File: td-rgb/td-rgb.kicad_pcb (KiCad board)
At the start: 2 copper layers, 65 x 29 mm, 26 parts, among them J1 ICD15S13E4GV00LF, J2 Conn_01x05_Male, J3 Conn_01x05_Male, J4 Conn_01x02_Male, SW1 SW_DPDT_x2, U1 LT1675CGNPBF, U2 LM2776

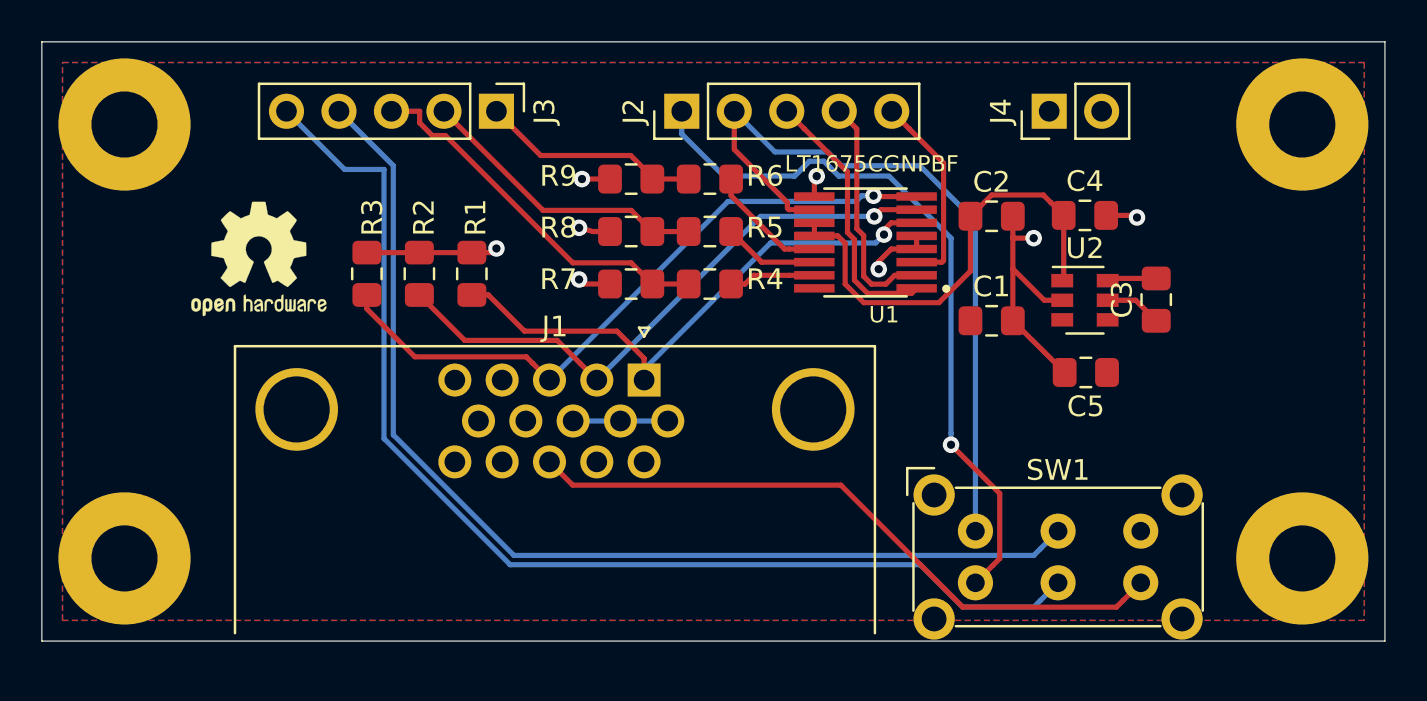
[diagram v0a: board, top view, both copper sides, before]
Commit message: Update footprint for DE-15 connector to correct pin row spacing
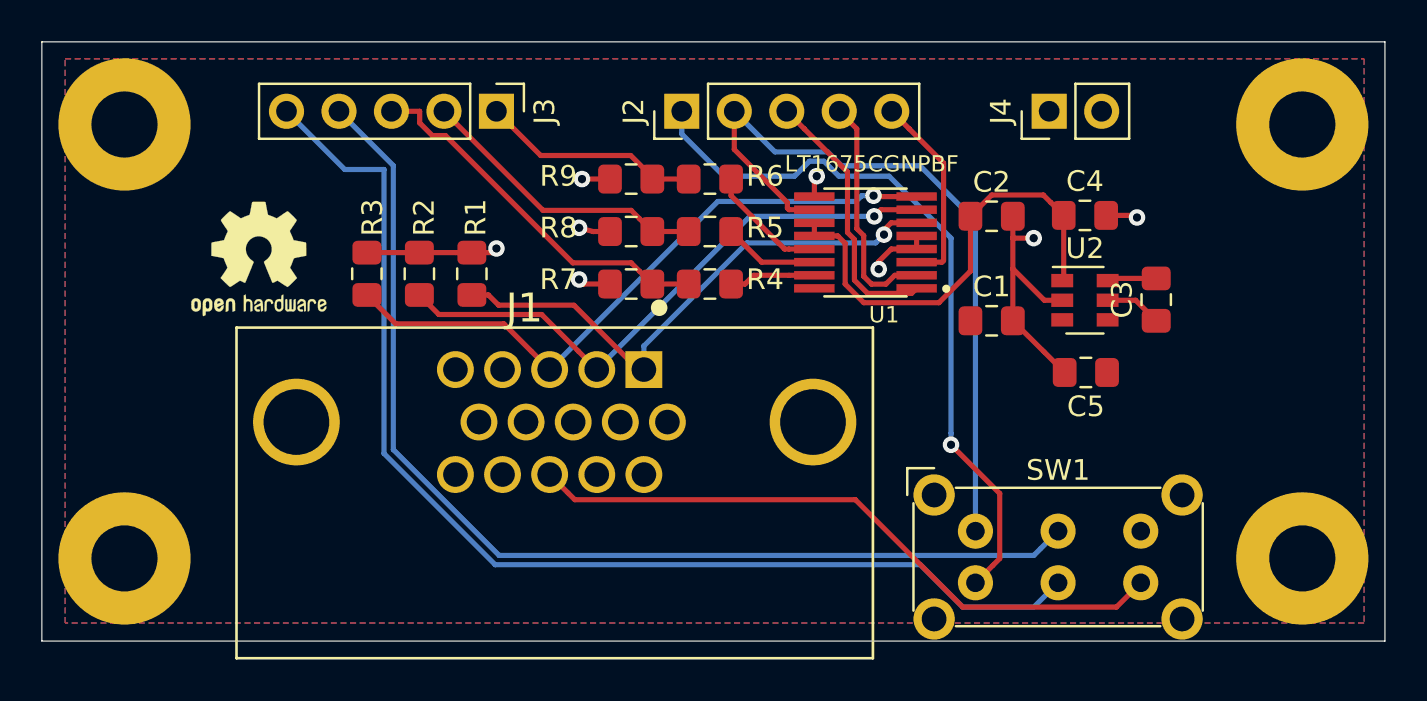
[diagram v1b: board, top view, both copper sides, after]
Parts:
- J1: footprint Connector_Dsub:DSUB-15-HD_Female_Horizontal_P2.29x1.98mm_EdgePinOffset8.35mm_Housed_MountingHolesOffset10.89mm -> 1-1734530-1:TE_1-1734530-1
- moved J1 4.78 mm to (134.8, 101.4)
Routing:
- net GND: track 33.7 -> 29.1 mm
- net /blue: track 32.4 -> 31.6 mm

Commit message: Correct DE-15 placement on PCB to bring closer to original design
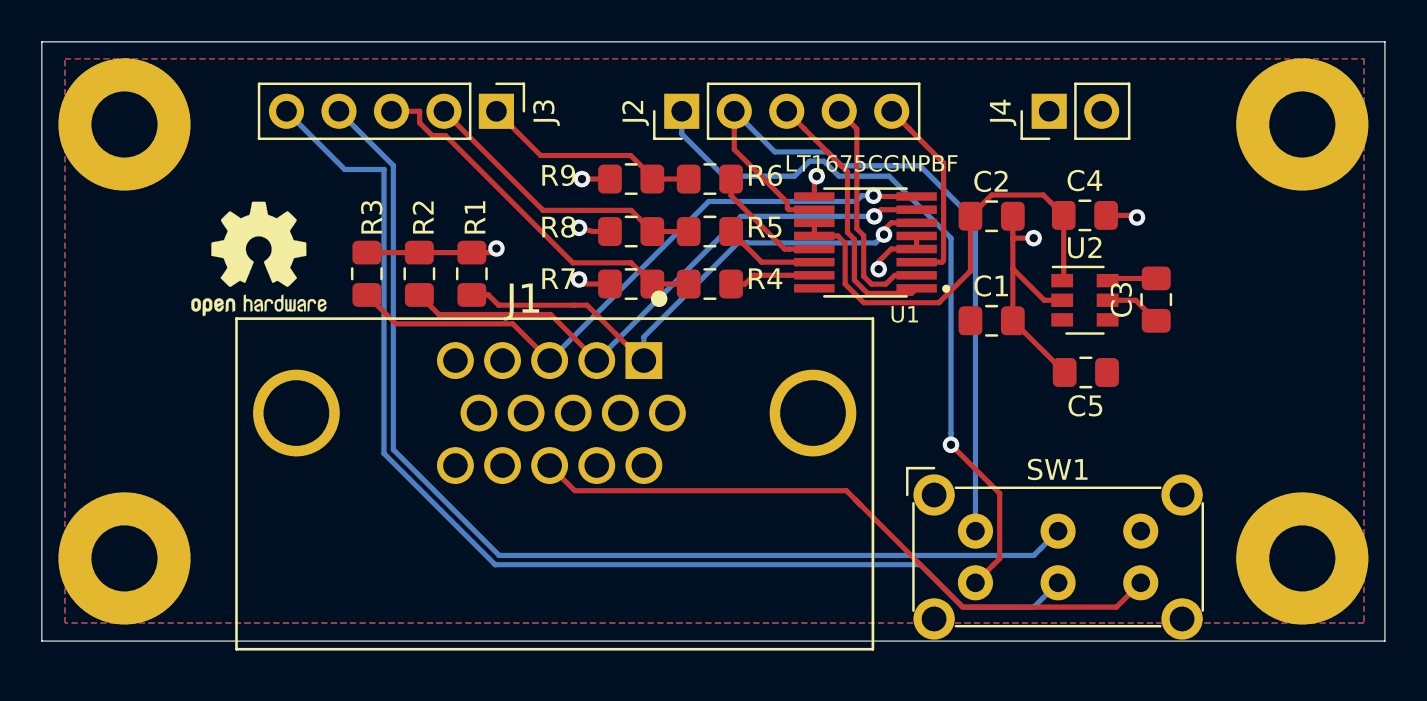
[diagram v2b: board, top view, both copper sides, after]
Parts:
- moved J1 0.44 mm to (134.8, 101.0)
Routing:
- net Net-(J1-Pad13): track 31.8 -> 32.3 mm
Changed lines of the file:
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@@
     (thickness 1.6)
     (drawings 19)
-    (tracks 184)
+    (tracks 187)
     (zones 0)
     (modules 26)
@@
   )
   (module 1-1734530-1:TE_1-1734530-1 (layer F.Cu)
-    (at 134.82 101.4)
+    (at 134.82 100.965)
     (fp_text reference J1 (at -1.47 -5.515) (layer F.SilkS)
       (effects (font (size 1.40272 1.40272) (thickness 0.05)))
@@
     (at 149.86 92.71 180)
     (attr smd)
-    (fp_text reference U1 (at -0.90029 -3.50115 180) (layer F.SilkS)
+    (fp_text reference U1 (at -1.905 -3.50115 180) (layer F.SilkS)
       (effects (font (size 0.787661 0.787661) (thickness 0.05)))
     )
@@
   (segment (start 148.52 92.3925) (end 148.874976 92.747476) (width 0.25) (layer F.Cu) (net 3))
   (segment (start 147.385 92.3925) (end 148.52 92.3925) (width 0.25) (layer F.Cu) (net 3))
-  (segment (start 135.467499 104.832499) (end 134.575 103.94) (width 0.25) (layer F.Cu) (net 6))
-  (segment (start 135.792501 105.157501) (end 135.467499 104.832499) (width 0.25) (layer F.Cu) (net 6))
-  (segment (start 149.370504 105.157501) (end 135.792501 105.157501) (width 0.25) (layer F.Cu) (net 6))
-  (segment (start 154.568004 110.355001) (end 149.370504 105.157501) (width 0.25) (layer F.Cu) (net 6))
   (segment (start 162.007 110.355001) (end 154.568004 110.355001) (width 0.25) (layer F.Cu) (net 6))
   (segment (start 163.182001 109.18) (end 162.007 110.355001) (width 0.25) (layer F.Cu) (net 6))
+  (segment (start 148.935504 104.722501) (end 149.623003 105.41) (width 0.25) (layer F.Cu) (net 6))
+  (segment (start 135.792501 104.722501) (end 148.935504 104.722501) (width 0.25) (layer F.Cu) (net 6))
+  (segment (start 134.575 103.505) (end 135.792501 104.722501) (width 0.25) (layer F.Cu) (net 6))
+  (segment (start 154.568004 110.355001) (end 149.623003 105.41) (width 0.25) (layer F.Cu) (net 6))
+  (segment (start 149.623003 105.41) (end 149.370504 105.157501) (width 0.25) (layer F.Cu) (net 6))
   (segment (start 152.335 90.4875) (end 150.291131 90.4875) (width 0.25) (layer F.Cu) (net 12))
   (segment (start 150.291131 90.4875) (end 150.250359 90.446728) (width 0.25) (layer F.Cu) (net 12))
   (via (at 150.250359 90.446728) (size 0.8) (drill 0.4) (layers F.Cu B.Cu) (net 12))
-  (segment (start 142.709999 90.725001) (end 134.575 98.86) (width 0.25) (layer B.Cu) (net 12))
-  (segment (start 149.406401 90.725001) (end 142.709999 90.725001) (width 0.25) (layer B.Cu) (net 12))
+  (segment (start 132.795732 96.645732) (end 134.575 98.425) (width 0.25) (layer F.Cu) (net 12))
+  (segment (start 125.73 95.25) (end 127.125732 96.645732) (width 0.25) (layer F.Cu) (net 12))
+  (segment (start 127.125732 96.645732) (end 132.795732 96.645732) (width 0.25) (layer F.Cu) (net 12))
+  (segment (start 142.274999 90.725001) (end 134.575 98.425) (width 0.25) (layer B.Cu) (net 12))
+  (segment (start 149.406401 90.725001) (end 142.274999 90.725001) (width 0.25) (layer B.Cu) (net 12))
   (segment (start 150.250359 90.446728) (end 149.684674 90.446728) (width 0.25) (layer B.Cu) (net 12))
   (segment (start 149.684674 90.446728) (end 149.406401 90.725001) (width 0.25) (layer B.Cu) (net 12))
-  (segment (start 133.682501 97.967501) (end 134.575 98.86) (width 0.25) (layer F.Cu) (net 12))
-  (segment (start 132.360732 96.645732) (end 133.682501 97.967501) (width 0.25) (layer F.Cu) (net 12))
-  (segment (start 127.125732 96.645732) (end 132.360732 96.645732) (width 0.25) (layer F.Cu) (net 12))
-  (segment (start 125.73 95.25) (end 127.125732 96.645732) (width 0.25) (layer F.Cu) (net 12))
   (segment (start 150.609696 91.1225) (end 150.286094 91.446102) (width 0.25) (layer F.Cu) (net 13))
   (via (at 150.286094 91.446102) (size 0.8) (drill 0.4) (layers F.Cu B.Cu) (net 13))
   (segment (start 152.335 91.1225) (end 150.609696 91.1225) (width 0.25) (layer F.Cu) (net 13))
-  (segment (start 144.268898 91.446102) (end 136.855 98.86) (width 0.25) (layer B.Cu) (net 13))
-  (segment (start 150.286094 91.446102) (end 144.268898 91.446102) (width 0.25) (layer B.Cu) (net 13))
-  (segment (start 135.962501 97.967501) (end 136.855 98.86) (width 0.25) (layer F.Cu) (net 13))
-  (segment (start 134.190722 96.195722) (end 135.962501 97.967501) (width 0.25) (layer F.Cu) (net 13))
-  (segment (start 129.215722 96.195722) (end 134.190722 96.195722) (width 0.25) (layer F.Cu) (net 13))
+  (segment (start 134.625722 96.195722) (end 136.855 98.425) (width 0.25) (layer F.Cu) (net 13))
   (segment (start 128.27 95.25) (end 129.215722 96.195722) (width 0.25) (layer F.Cu) (net 13))
+  (segment (start 129.215722 96.195722) (end 134.625722 96.195722) (width 0.25) (layer F.Cu) (net 13))
+  (segment (start 143.833898 91.446102) (end 136.855 98.425) (width 0.25) (layer B.Cu) (net 13))
+  (segment (start 150.286094 91.446102) (end 143.833898 91.446102) (width 0.25) (layer B.Cu) (net 13))
   (segment (start 152.335 91.7575) (end 151.105 91.7575) (width 0.25) (layer F.Cu) (net 14))
   (segment (start 151.105 91.7575) (end 150.754988 92.107512) (width 0.25) (layer F.Cu) (net 14))
   (via (at 150.754988 92.329357) (size 0.8) (drill 0.4) (layers F.Cu B.Cu) (net 14))
   (segment (start 150.754988 92.107512) (end 150.754988 92.329357) (width 0.25) (layer F.Cu) (net 14))
-  (segment (start 139.147001 99.368339) (end 139.147001 98.852999) (width 0.25) (layer B.Cu) (net 14))
   (segment (start 139.135 97.7175) (end 139.135 98.86) (width 0.25) (layer B.Cu) (net 14))
-  (segment (start 144.123144 92.729356) (end 139.135 97.7175) (width 0.25) (layer B.Cu) (net 14))
-  (segment (start 150.354989 92.729356) (end 144.123144 92.729356) (width 0.25) (layer B.Cu) (net 14))
-  (segment (start 150.754988 92.329357) (end 150.354989 92.729356) (width 0.25) (layer B.Cu) (net 14))
   (segment (start 138.865 98.86) (end 139.135 98.86) (width 0.25) (layer F.Cu) (net 14))
-  (segment (start 135.750712 95.745712) (end 138.865 98.86) (width 0.25) (layer F.Cu) (net 14))
   (segment (start 132.105712 95.745712) (end 135.750712 95.745712) (width 0.25) (layer F.Cu) (net 14))
   (segment (start 130.81 95.25) (end 131.61 95.25) (width 0.25) (layer F.Cu) (net 14))
   (segment (start 131.61 95.25) (end 132.105712 95.745712) (width 0.25) (layer F.Cu) (net 14))
+  (segment (start 135.750712 95.745712) (end 136.385712 95.745712) (width 0.25) (layer F.Cu) (net 14))
+  (segment (start 136.385712 95.745712) (end 137.795 97.155) (width 0.25) (layer F.Cu) (net 14))
+  (segment (start 137.795 97.155) (end 138.43 97.79) (width 0.25) (layer F.Cu) (net 14))
+  (segment (start 144.123144 92.729356) (end 144.123144 92.731856) (width 0.25) (layer B.Cu) (net 14))
+  (segment (start 150.354989 92.729356) (end 144.123144 92.729356) (width 0.25) (layer B.Cu) (net 14))
+  (segment (start 150.754988 92.329357) (end 150.354989 92.729356) (width 0.25) (layer B.Cu) (net 14))
+  (segment (start 143.688144 92.729356) (end 144.123144 92.729356) (width 0.25) (layer B.Cu) (net 14))
+  (segment (start 139.135 97.2825) (end 143.688144 92.729356) (width 0.25) (layer B.Cu) (net 14))
+  (segment (start 139.135 98.425) (end 139.135 97.2825) (width 0.25) (layer B.Cu) (net 14))
   (via (at 154 102.5) (size 0.8) (drill 0.4) (layers F.Cu B.Cu) (net 15))
   (segment (start 156.357002 108.004999) (end 156.032 108.330001) (width 0.25) (layer F.Cu) (net 15))
@@
   (segment (start 155.182001 105.477919) (end 155.182001 106.68) (width 0.25) (layer B.Cu) (net 29))
   (segment (start 155.182001 91.682001) (end 155.182001 105.477919) (width 0.25) (layer B.Cu) (net 29))
-  (zone (net 2) (net_name +5V) (layer F.Cu) (hatch edge 0.508)
+  (zone (net 1) (net_name GND) (layer B.Cu) (hatch edge 0.508)
     (connect_pads (clearance 0.2))
     (min_thickness 0.254)
@@
     )
   )
-  (zone (net 1) (net_name GND) (layer B.Cu) (hatch edge 0.508)
+  (zone (net 2) (net_name +5V) (layer F.Cu) (hatch edge 0.508)
     (connect_pads (clearance 0.2))
     (min_thickness 0.254)
